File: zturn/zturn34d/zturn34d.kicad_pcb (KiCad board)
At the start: 4 copper layers, 59.7 x 54 mm, 20 parts, among them Q1 SSM6N15AFU, Q2 SSM6N15AFU, Q3 SSM6N15AFU, Q4 SSM6N15AFU, Q5 SSM6N15AFU, Q6 SSM6N15AFU, Q7 SSM6N15AFU, Q8 SSM6N15AFU

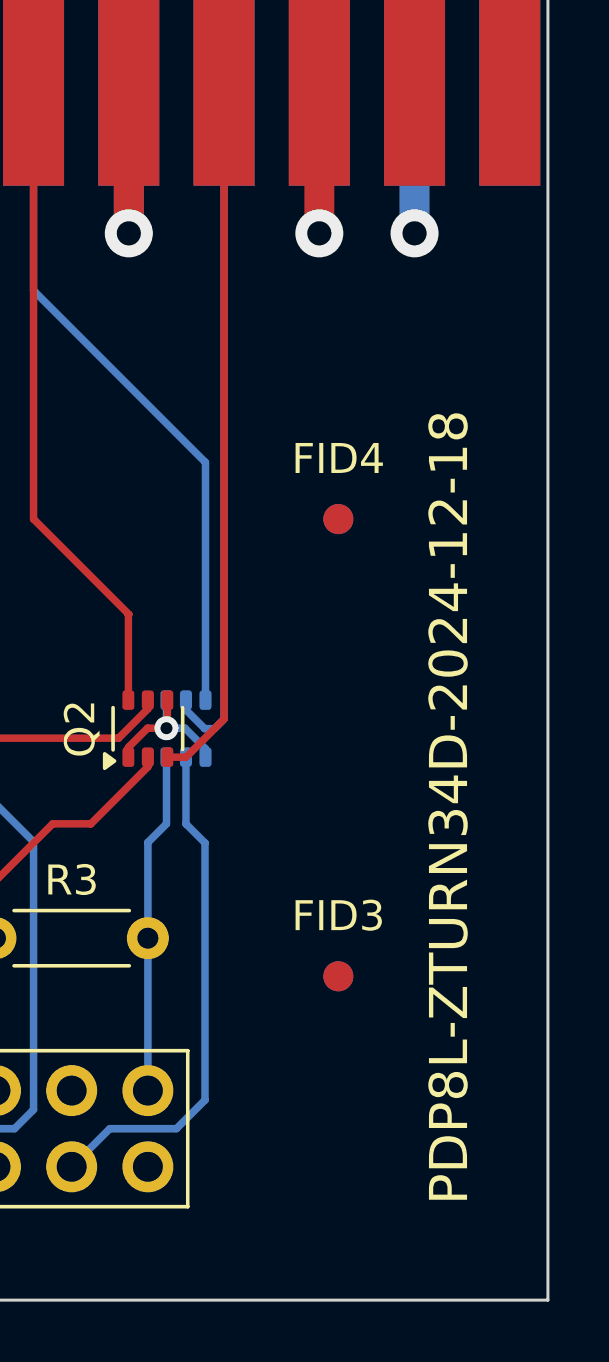
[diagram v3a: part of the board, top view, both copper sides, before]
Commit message: add I2C circuit to zturn boardset to operate front panel board
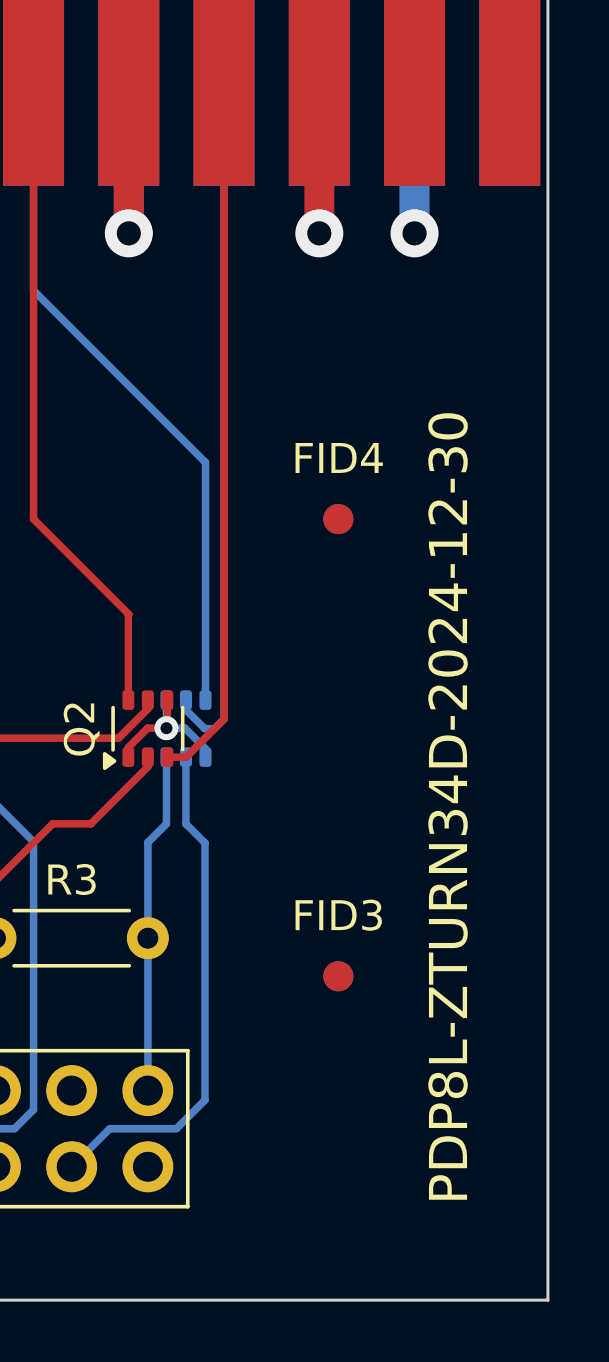
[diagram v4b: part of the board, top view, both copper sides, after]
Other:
- board text added: "PDP8L-ZTURN34D-2024-12-30"
- board text removed: "PDP8L-ZTURN34D-2024-12-18"
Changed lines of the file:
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@@
     (pad_to_mask_clearance 0)
     (pcbplotparams
-      (layerselection 0x003d0ff_ffffffff)
+      (layerselection 0x003f0ff_ffffffff)
       (plot_on_all_layers_selection 0x0000000_00000000)
       (disableapertmacros false)
@@
   (gr_line (start 59.69 53.975) (end 0 53.975)
     (stroke (width 0.1) (type default)) (layer "Edge.Cuts"))
-  (gr_text "PDP8L-ZTURN34D-2024-12-18" (at 57.15 50.8 90) (layer "F.SilkS")
+  (gr_text "PDP8L-ZTURN34D-2024-12-30" (at 57.15 50.8 90) (layer "F.SilkS")
     (effects (font (size 1.27 1.27) (thickness 0.15)) (justify left bottom))
   )
